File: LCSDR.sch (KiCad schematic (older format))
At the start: 10 parts, among them J10 Conn_01x01, J11 Conn_01x01, J14 I2C, J2 IDC10 Serial Wire, J5 IQ_IN, J6 IQ_OUT, J7 CLK, J8 Conn_01x01, J9 Conn_01x01

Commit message: add I2S_CLKIN_MCU
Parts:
- removed J14: I2C, Pin_Headers:Pin_Header_Straight_1x03_Pitch2.54mm, symbol Conn_01x03
- removed J2: IDC10 Serial Wire, UI:USBBLASTER, symbol Conn_02x05_Odd_Even
- removed J5: IQ_IN, Pin_Headers:Pin_Header_Straight_1x03_Pitch2.54mm, symbol Conn_01x03
- removed J6: IQ_OUT, Pin_Headers:Pin_Header_Straight_1x03_Pitch2.54mm, symbol Conn_01x03
- removed J7: CLK, Pin_Headers:Pin_Header_Straight_1x06_Pitch2.54mm, symbol Conn_01x06
- removed RN1: 47, Resistors_SMD:R_Array_Convex_4x0603, symbol R_Pack04
- added J2, J4: Conn_01x30, Pin_Headers:Pin_Header_Straight_1x30_Pitch2.54mm, symbol Conn_01x30
- added RN4, RN5: 47, Resistors_SMD:R_Array_Convex_4x0603, symbol R_Pack04
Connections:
- net CLK0: now also J2.6 (Pin_6)
- net CLK1: now also J2.4 (Pin_4)
- net CLK2: now also J2.2 (Pin_2)
- net GND: now also J2.1 (Pin_1), J2.20 (Pin_20), J2.3 (Pin_3), J2.5 (Pin_5), J4.10 (Pin_10), J4.11 (Pin_11), J4.12 (Pin_12), J4.13 (Pin_13), J4.15 (Pin_15), J4.17 (Pin_17), J4.19 (Pin_19)
- net I2C_SCL: now also J2.18 (Pin_18)
- net I2C_SDA: now also J2.19 (Pin_19)
- new net: J4.1 (Pin_1), RN4.5 (R4.2)
- new net: J4.2 (Pin_2), RN4.6 (R3.2)
- new net: J4.3 (Pin_3), RN4.7 (R2.2)
- new net: J4.4 (Pin_4), RN4.8 (R1.2)
- new net: J4.5 (Pin_5), RN5.5 (R4.2)
- new net: J4.6 (Pin_6), RN5.6 (R3.2)
- new net: J4.7 (Pin_7), RN5.7 (R2.2)
- new net: J4.8 (Pin_8), RN5.8 (R1.2)
- new net ADC: J4.9 (Pin_9)
- new net IO0: RN4.4 (R4.1)
- new net IO1: RN4.3 (R3.1)
- new net IO2: RN4.2 (R2.1)
- new net IO3: RN4.1 (R1.1)
- new net IO4: RN5.4 (R4.1)
- new net IO5: RN5.3 (R3.1)
- new net IO6: RN5.2 (R2.1)
- new net IO7: RN5.1 (R1.1)
- new net LINE_OUT_LEFT: J4.18 (Pin_18)
- new net LINE_OUT_RIGHT: J4.20 (Pin_20)

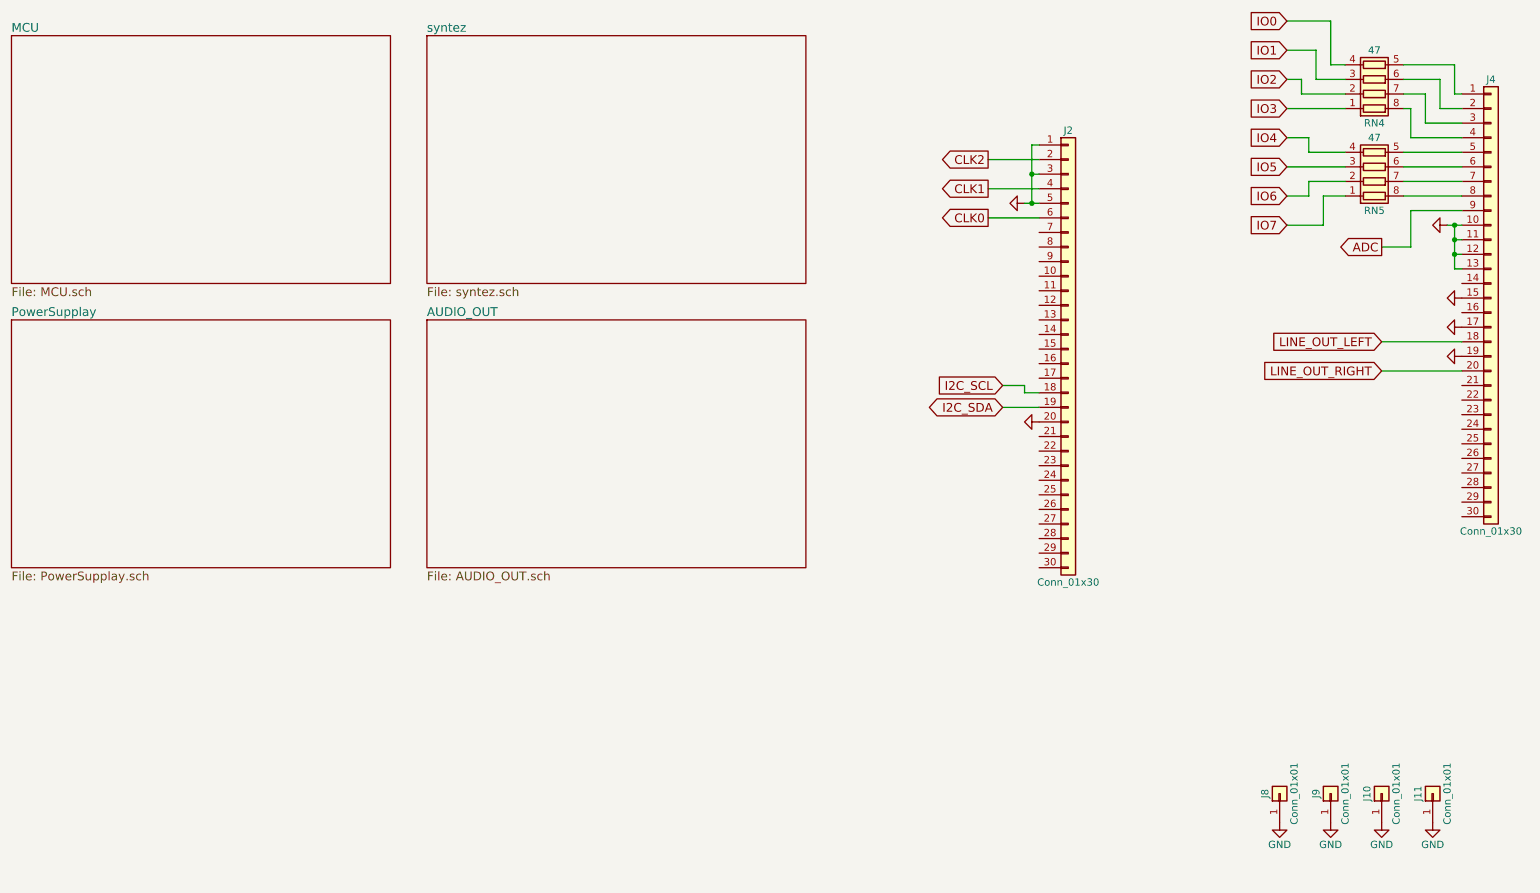
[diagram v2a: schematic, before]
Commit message: PCB almost ready, needs some GND vias
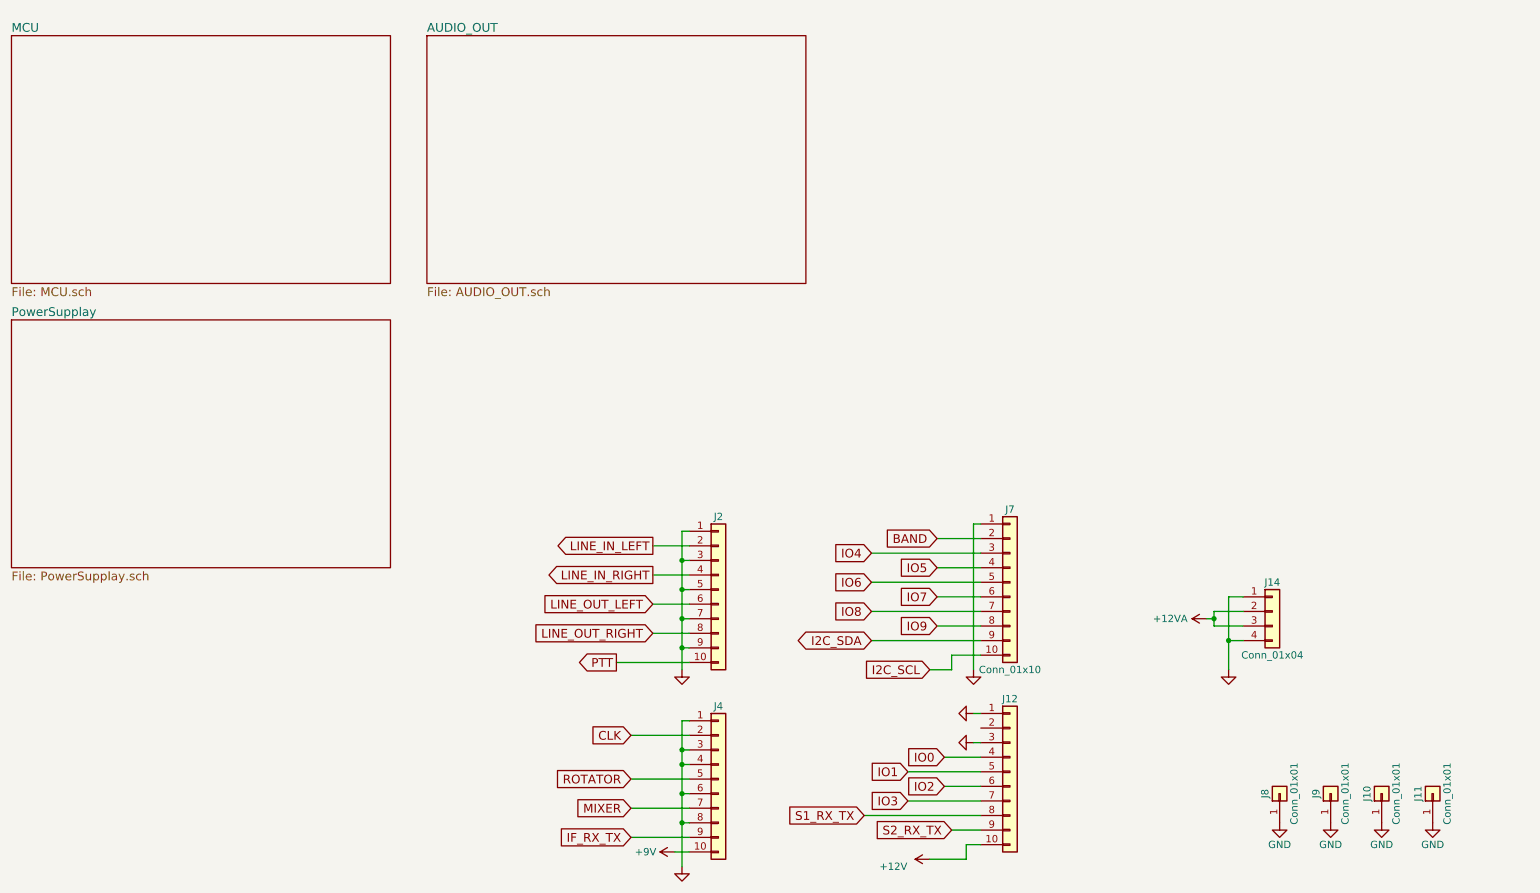
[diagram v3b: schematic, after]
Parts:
- removed J2, J4: Conn_01x30, Pin_Headers:Pin_Header_Straight_1x30_Pitch2.54mm, symbol Conn_01x30
- removed RN4, RN5: 47, Resistors_SMD:R_Array_Convex_4x0603, symbol R_Pack04
- added J12, J2, J4, J7: Conn_01x10, Pin_Headers:Pin_Header_Straight_1x10_Pitch2.54mm, symbol Conn_01x10
- added J14: Conn_01x04, Pin_Headers:Pin_Header_Straight_1x04_Pitch2.54mm, symbol Conn_01x04
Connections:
- net GND: now also J12.1 (Pin_1), J12.3 (Pin_3), J14.1 (Pin_1), J14.4 (Pin_4), J2.1 (Pin_1), J2.3 (Pin_3), J2.5 (Pin_5), J2.7 (Pin_7), J2.9 (Pin_9), J4.1 (Pin_1), J4.3 (Pin_3), J4.4 (Pin_4), J4.6 (Pin_6), J4.8 (Pin_8), J7.1 (Pin_1)
- net I2C_SCL: now also J7.10 (Pin_10)
- net I2C_SDA: now also J7.9 (Pin_9)
- net IO0: now also J12.4 (Pin_4)
- net IO1: now also J12.5 (Pin_5)
- net IO2: now also J12.6 (Pin_6)
- net IO3: now also J12.7 (Pin_7)
- net IO4: now also J7.3 (Pin_3)
- net IO5: now also J7.4 (Pin_4)
- net IO6: now also J7.5 (Pin_5)
- net IO7: now also J7.6 (Pin_6)
- net LINE_OUT_LEFT: now also J2.6 (Pin_6)
- net LINE_OUT_RIGHT: now also J2.8 (Pin_8)
- new net +12V: J12.10 (Pin_10)
- new net +12VA: J14.2 (Pin_2), J14.3 (Pin_3)
- new net +9V: J4.10 (Pin_10)
- new net BAND: J7.2 (Pin_2)
- new net CLK: J4.2 (Pin_2)
- new net IF_RX_TX: J4.9 (Pin_9)
- new net IO8: J7.7 (Pin_7)
- new net IO9: J7.8 (Pin_8)
- new net LINE_IN_LEFT: J2.2 (Pin_2)
- new net LINE_IN_RIGHT: J2.4 (Pin_4)
- new net MIXER: J4.7 (Pin_7)
- new net PTT: J2.10 (Pin_10)
- new net ROTATOR: J4.5 (Pin_5)
- new net S1_RX_TX: J12.8 (Pin_8)
- new net S2_RX_TX: J12.9 (Pin_9)

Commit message: edit
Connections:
- net IO4 is gone; now on net GND: J7.3 (Pin_3)
- net IO6 is gone; now on net GND: J7.5 (Pin_5)
- net IO5 renamed BPF
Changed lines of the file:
@@
 Wire Wire Line
 	7200 5100 7050 5100
-Text GLabel 6650 4300 0    60   Input ~ 0
-IO4
-Wire Wire Line
-	6650 4300 7400 4300
-Wire Wire Line
-	7400 4400 7100 4400
-Text GLabel 7100 4400 0    60   Input ~ 0
-IO5
-Text GLabel 6650 4500 0    60   Input ~ 0
-IO6
-Wire Wire Line
-	6650 4500 7400 4500
 Text GLabel 7100 4600 0    60   Input ~ 0
 IO7
@@
 Text GLabel 6650 4700 0    60   Input ~ 0
 IO8
+Wire Wire Line
+	7400 4300 7350 4300
+Connection ~ 7350 4300
+Wire Wire Line
+	7400 4500 7350 4500
+Connection ~ 7350 4500
+Text GLabel 7100 4400 0    60   BiDi ~ 0
+BPF
+Wire Wire Line
+	7400 4400 7100 4400
 $EndSCHEMATC
